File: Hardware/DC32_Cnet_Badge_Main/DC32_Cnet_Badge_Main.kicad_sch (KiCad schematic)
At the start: 8 parts, among them J1 SAO_Conn, J3 Conn_01x02_Male, U2 MH-CD42_LiPo_Batery_Managemen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

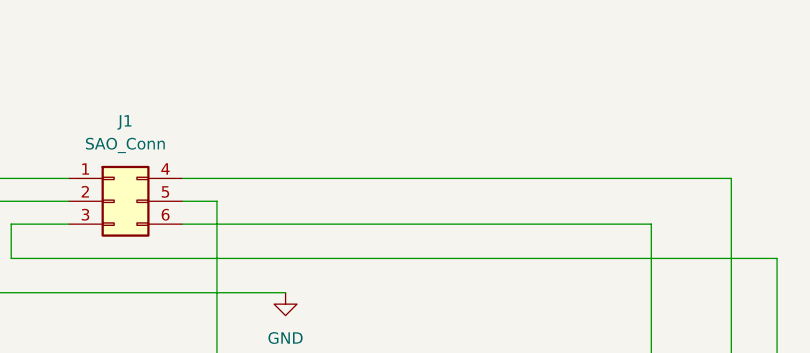
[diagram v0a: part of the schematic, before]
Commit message: Updated schematics and generated PDFs
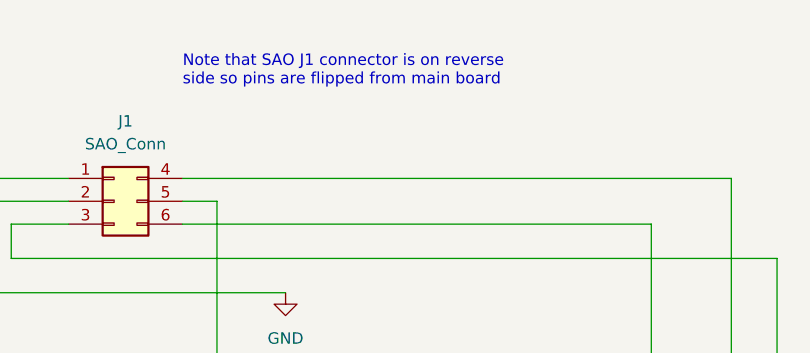
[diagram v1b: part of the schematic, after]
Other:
- note added: "Note that SAO J1 connector is on reverse side so pins are flipped from main board"
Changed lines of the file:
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@@
     (stroke (width 0) (type default))
+  )
+  (text "Note that SAO J1 connector is on reverse\nside so pins are flipped from main board"
+    (at 165.1 29.21 0)
+    (effects (font (size 1.27 1.27)) (justify left bottom))
   )
   (label "PLAYPIN" (at 246.38 107.95 0) (fields_autoplaced)
